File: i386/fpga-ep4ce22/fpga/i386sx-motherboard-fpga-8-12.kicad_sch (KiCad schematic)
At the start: 1 part, among them U3 (2/6) EP4CE22F17C8N

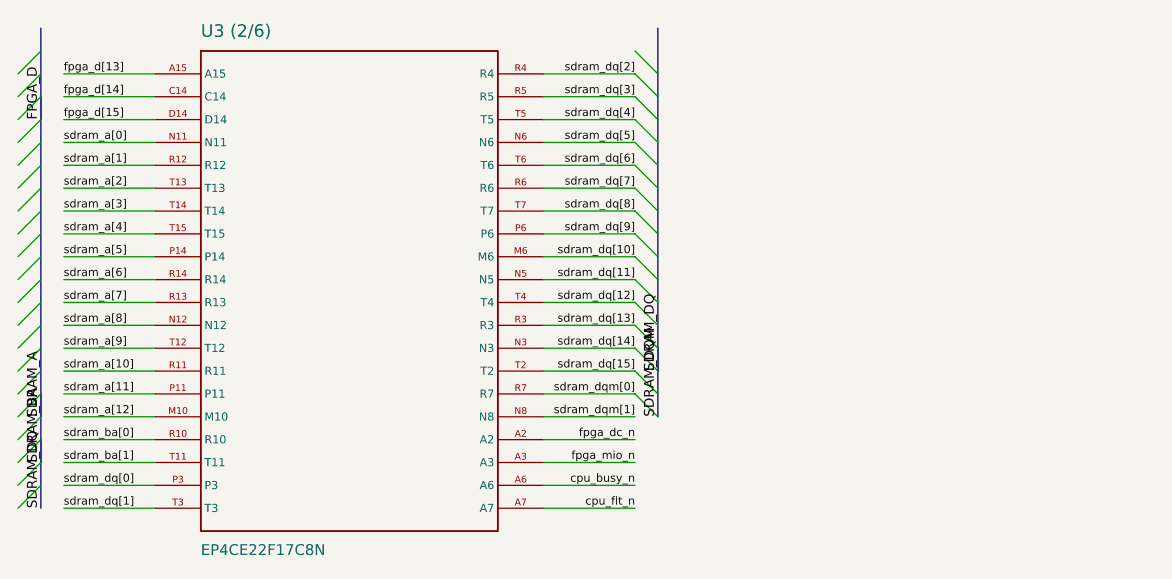
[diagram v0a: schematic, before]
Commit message: Publish the motherboards' KiCad files
From socket3@c0f6464 socket7@9205469 socket370@524f5b1 i386@bea926c
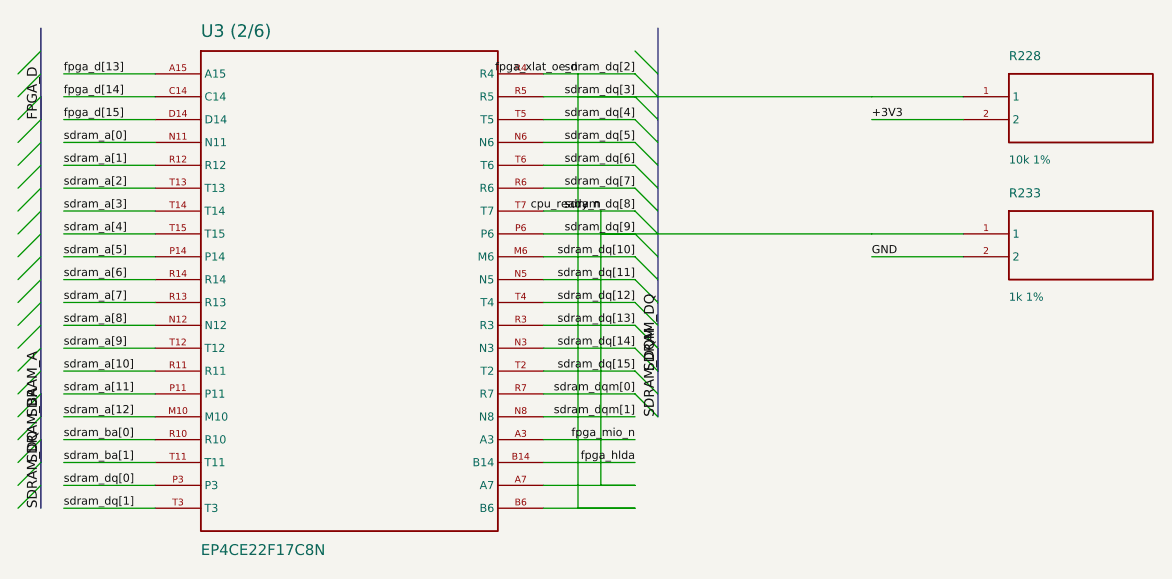
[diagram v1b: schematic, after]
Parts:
- added R228: 10k 1%, symbol gen:S2_0s
- added R233: 1k 1%, symbol gen:S2_0s
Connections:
- net sdram_dq[3] is gone; now on net fpga_xlat_oe_n: U3 (2/6).R5
- net sdram_dq[8] is gone; now on net cpu_ready_n: U3 (2/6).T7
- net sdram_dq[9] is gone; now on net cpu_ready_n: U3 (2/6).P6
- removed net cpu_busy_n: U3 (2/6).A6
- net cpu_flt_n renamed cpu_ready_n
- net cpu_ready_n: now also R233.1
- removed net fpga_dc_n: U3 (2/6).A2
- net sdram_dq[2] renamed fpga_xlat_oe_n
- net fpga_xlat_oe_n: now also U3 (2/6).B6, R228.1
- new net +3V3: R228.2
- new net GND: R233.2
- new net fpga_hlda: U3 (2/6).B14
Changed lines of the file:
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@@
     (property "Reference" "U3 (2/6)" (at 44.46 17.65 0) (effects (font (size 1.4 1.4)) (justify left bottom)))
     (property "Value" "EP4CE22F17C8N" (at 44.46 73.79 0) (effects (font (size 1.2 1.2)) (justify left top)))
-    (instances (project "i386sx-motherboard" (path "/0ac398a9-1d89-4090-a36f-db7b4d3d6c0d/704bdeab-79ba-40f8-8559-3b5ffedcd0d7" (reference "U3") (unit 1))))
+    (instances (project "i386sx-motherboard" (path "/ea05416d-ce24-4c39-9113-85b33d9a88b0/66fb382b-29d7-4d43-a7ff-45fa9e692e96" (reference "U3") (unit 1))))
   )
   (bus (pts (xy 26.68 16.51) (xy 26.68 26.67)) (stroke (width 0) (type default)))
@@
   (bus_entry (at 92.70 54.61) (size 2.54 2.54) (stroke (width 0) (type default)))
   (bus_entry (at 92.70 57.15) (size 2.54 2.54) (stroke (width 0) (type default)))
+  (symbol (lib_id "gen:S2_0s") (at 142.24 25.40 0) (unit 1) (exclude_from_sim no) (in_bom yes) (on_board yes) (dnp no)
+    (property "Reference" "R228" (at 134.24 20.19 0) (effects (font (size 1.0 1.0)) (justify left bottom)))
+    (property "Value" "10k 1%" (at 134.24 30.61 0) (effects (font (size 0.9 0.9)) (justify left top)))
+    (instances (project "i386sx-motherboard" (path "/ea05416d-ce24-4c39-9113-85b33d9a88b0/66fb382b-29d7-4d43-a7ff-45fa9e692e96" (reference "R228") (unit 1))))
+  )
+  (symbol (lib_id "gen:S2_0s") (at 142.24 40.64 0) (unit 1) (exclude_from_sim no) (in_bom yes) (on_board yes) (dnp no)
+    (property "Reference" "R233" (at 134.24 35.43 0) (effects (font (size 1.0 1.0)) (justify left bottom)))
+    (property "Value" "1k 1%" (at 134.24 45.85 0) (effects (font (size 0.9 0.9)) (justify left top)))
+    (instances (project "i386sx-motherboard" (path "/ea05416d-ce24-4c39-9113-85b33d9a88b0/66fb382b-29d7-4d43-a7ff-45fa9e692e96" (reference "R233") (unit 1))))
+  )
   (wire (pts (xy 39.38 21.59) (xy 29.22 21.59)) (stroke (width 0) (type default)))
   (wire (pts (xy 39.38 24.13) (xy 29.22 24.13)) (stroke (width 0) (type default)))
@@
   (wire (pts (xy 82.54 67.31) (xy 92.70 67.31)) (stroke (width 0) (type default)))
   (wire (pts (xy 82.54 69.85) (xy 92.70 69.85)) (stroke (width 0) (type default)))
+  (wire (pts (xy 129.16 24.13) (xy 119.00 24.13)) (stroke (width 0) (type default)))
+  (wire (pts (xy 129.16 26.67) (xy 119.00 26.67)) (stroke (width 0) (type default)))
+  (wire (pts (xy 129.16 39.37) (xy 119.00 39.37)) (stroke (width 0) (type default)))
+  (wire (pts (xy 129.16 41.91) (xy 119.00 41.91)) (stroke (width 0) (type default)))
+  (wire (pts (xy 88.90 39.37) (xy 88.90 67.31)) (stroke (width 0) (type default)))
+  (wire (pts (xy 92.70 67.31) (xy 88.90 67.31)) (stroke (width 0) (type default)))
+  (wire (pts (xy 119.00 39.37) (xy 88.90 39.37)) (stroke (width 0) (type default)))
+  (wire (pts (xy 88.90 36.83) (xy 88.90 39.37)) (stroke (width 0) (type default)))
+  (wire (pts (xy 86.36 24.13) (xy 86.36 69.85)) (stroke (width 0) (type default)))
+  (wire (pts (xy 92.70 69.85) (xy 86.36 69.85)) (stroke (width 0) (type default)))
+  (wire (pts (xy 119.00 24.13) (xy 86.36 24.13)) (stroke (width 0) (type default)))
+  (wire (pts (xy 86.36 21.59) (xy 86.36 24.13)) (stroke (width 0) (type default)))
   (label "fpga_d[13]" (at 29.22 21.59 0) (effects (font (size 0.9 0.9)) (justify left bottom)))
   (label "fpga_d[14]" (at 29.22 24.13 0) (effects (font (size 0.9 0.9)) (justify left bottom)))
@@
   (label "sdram_dqm[0]" (at 92.70 57.15 0) (effects (font (size 0.9 0.9)) (justify right bottom)))
   (label "sdram_dqm[1]" (at 92.70 59.69 0) (effects (font (size 0.9 0.9)) (justify right bottom)))
-  (label "fpga_dc_n" (at 92.70 62.23 0) (effects (font (size 0.9 0.9)) (justify right bottom)))
-  (label "fpga_mio_n" (at 92.70 64.77 0) (effects (font (size 0.9 0.9)) (justify right bottom)))
-  (label "cpu_busy_n" (at 92.70 67.31 0) (effects (font (size 0.9 0.9)) (justify right bottom)))
-  (label "cpu_flt_n" (at 92.70 69.85 0) (effects (font (size 0.9 0.9)) (justify right bottom)))
+  (label "cpu_ready_n" (at 88.90 36.83 0) (effects (font (size 0.9 0.9)) (justify right bottom)))
+  (label "fpga_xlat_oe_n" (at 86.36 21.59 0) (effects (font (size 0.9 0.9)) (justify right bottom)))
+  (label "fpga_mio_n" (at 92.70 62.23 0) (effects (font (size 0.9 0.9)) (justify right bottom)))
+  (label "fpga_hlda" (at 92.70 64.77 0) (effects (font (size 0.9 0.9)) (justify right bottom)))
+  (label "+3V3" (at 119.00 26.67 0) (effects (font (size 0.9 0.9)) (justify left bottom)))
+  (label "GND" (at 119.00 41.91 0) (effects (font (size 0.9 0.9)) (justify left bottom)))
 )
